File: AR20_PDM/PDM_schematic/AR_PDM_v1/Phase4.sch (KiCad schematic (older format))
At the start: 22 parts, among them Q1 BTS50025-1TAD, U1 INA233

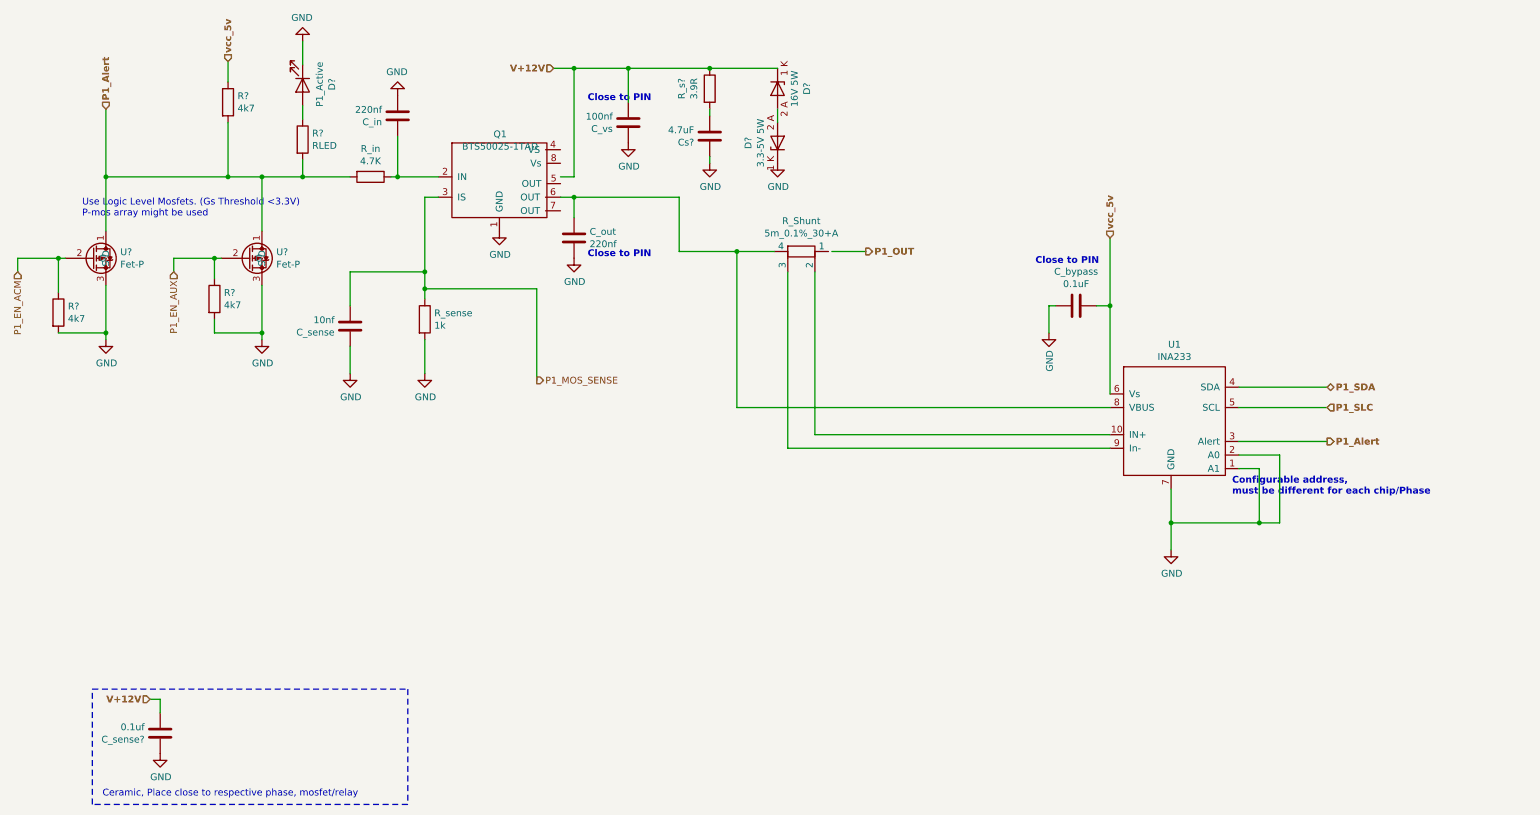
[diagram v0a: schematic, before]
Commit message: Major Schematics changes-work in progress
- Added rest of the phases
- Corrected pin names, and began to connect everything
- Began mapping the connectors, Pin-out not yet verified for all connectors
- Began mapping of user interface (Led indicators)
- INA233 now senses OUT voltage on mosfets instead of main 12Volt
- Added extra decoupling capacitors
Known things to fix:
- AUX inputs activation method, and a disconnect switch on phase 1-7 (mosfets)
- Rest of the user interface
- Find correct plugs for the system
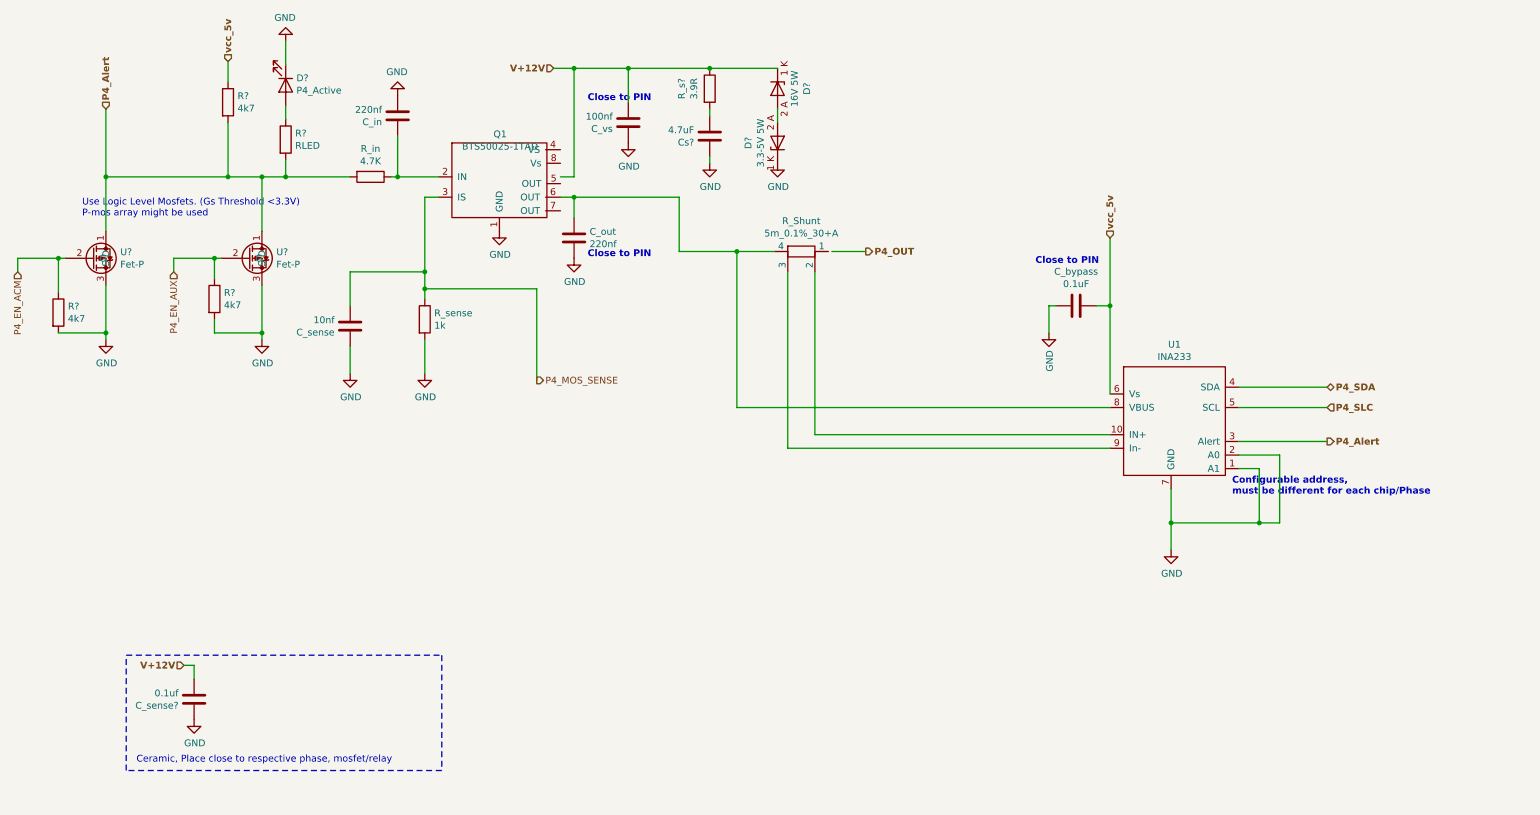
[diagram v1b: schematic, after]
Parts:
- removed C_sense?: 0.1uf, symbol AR20_PDM_v1-rescue:C-Device
- removed D?: P1_Active, symbol Device:LED
- removed R?: RLED, symbol AR20_PDM_v1-rescue:R-Device
- added C_sense?: 0.1uf, symbol AR20_PDM_v1-rescue:C-Device
- added D?: P4_Active, symbol Device:LED
- added R?: RLED, symbol AR20_PDM_v1-rescue:R-Device
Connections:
- net GND: now also C_sense?.1, D?.1 (K)
- net V+12V: now also C_sense?.2
- net P1_Alert renamed P4_Alert
- net P4_Alert: now also R?.2
- net P1_EN_ACM renamed P4_EN_ACM
- net P1_EN_AUX renamed P4_EN_AUX
- net P1_MOS_SENSE renamed P4_MOS_SENSE
- net P1_SDA renamed P4_SDA
- net P1_SLC renamed P4_SLC
- new net: D?.2 (A), R?.1

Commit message: Added LEDs and switches.
- Added all status leds
- Added all switches
- ! Connections are work in progress, not everything is correct
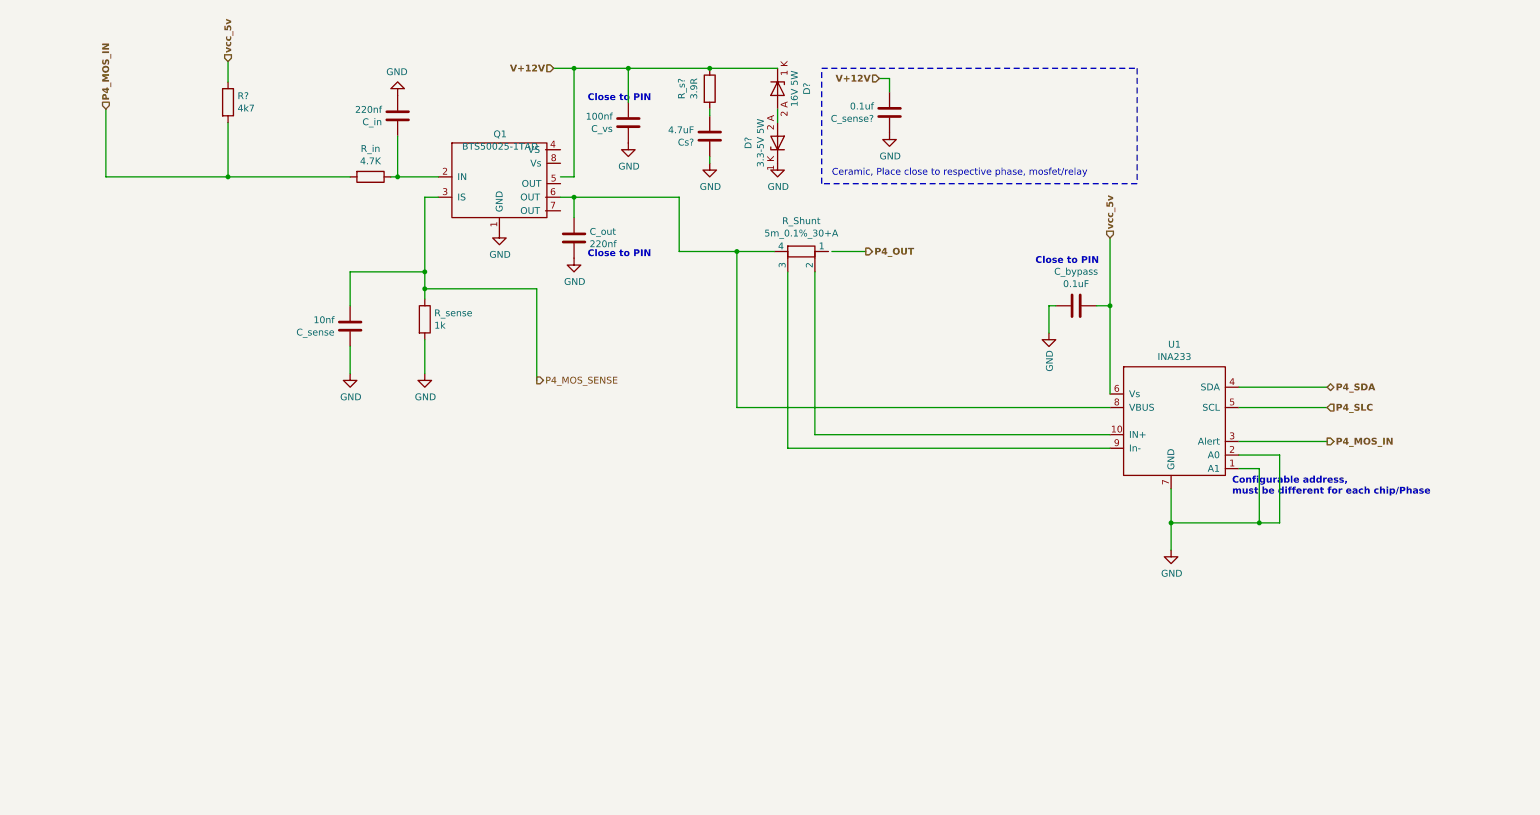
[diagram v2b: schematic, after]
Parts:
- removed D?: P4_Active, symbol Device:LED
- removed R? (x2): 4k7, symbol AR20_PDM_v1-rescue:R-Device
- removed R?: RLED, symbol AR20_PDM_v1-rescue:R-Device
- removed U? (x2): Fet-P, symbol AR20_PDM_v1-rescue:GenericFet-P
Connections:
- net labels added: P4_MOS_IN
- net labels removed: P4_Alert, P4_EN_ACM, P4_EN_AUX
- wire segments 81 -> 59
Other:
- note removed: "Use Logic Level Mosfets. (Gs Threshold <3.3V)\nP-mos array might be used"
- moved on the sheet: C_sense?

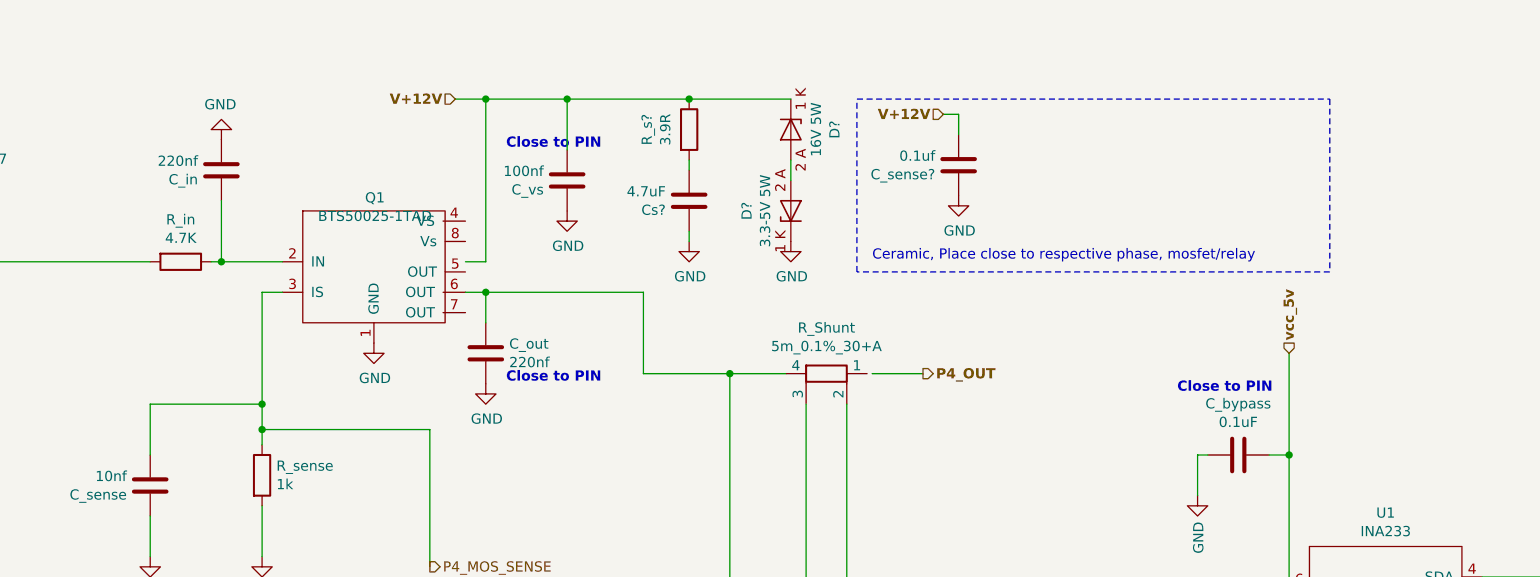
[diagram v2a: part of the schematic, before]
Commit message: Fixed wrong value components and ports, wiring, see discription
- Fixed supply cappacitor value 220 nf to 100nf
- Fixed IN cappacitor value 220 nf to 150 nf
- Fixed out cappacitor value, 220nf to 10 nf
- Made a mux for mosfet sense
- Found a I/O port expander
- Added some and removed some leds
- Fixed all labels, and wired everything up, besides the connectors
- Still missing connector and acm connector pinout.
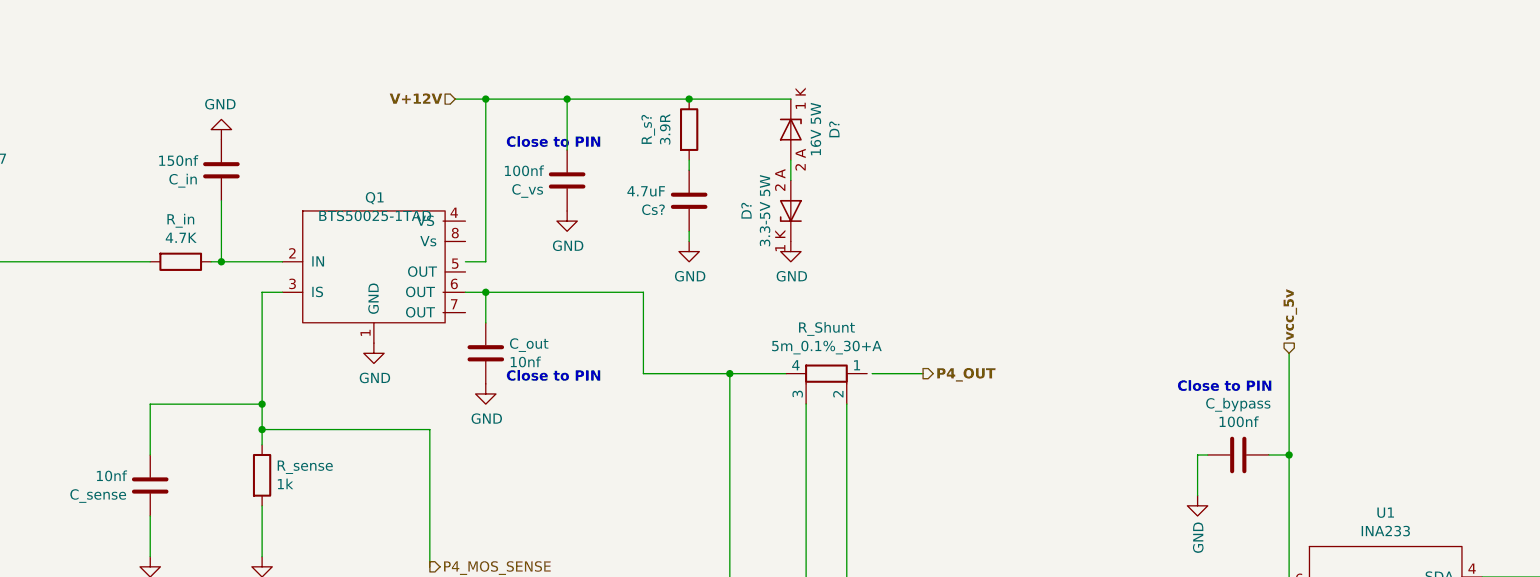
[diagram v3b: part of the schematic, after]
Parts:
- removed C_sense?: 0.1uf, symbol AR20_PDM_v1-rescue:C-Device
- C_bypass: value 0.1uF -> 100nf
- C_in: value 220nf -> 150nf
- C_out: value 220nf -> 10nf
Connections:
- wire segments 59 -> 57
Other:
- note removed: "Ceramic, Place close to respective phase, mosfet/relay"
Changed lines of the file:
@@
 $Descr A4 11693 8268
 encoding utf-8
-Sheet 9 11
+Sheet 9 13
 Title ""
 Date ""
@@
 AR Path="/5E10174B/5DAAC1D1" Ref="C_out?"  Part="1"
 F 0 "C_out?" H 4915 2896 50  0000 L CNN
-F 1 "220nf" H 4915 2805 50  0000 L CNN
+F 1 "10nf" H 4915 2805 50  0000 L CNN
 F 2 "" H 4838 2700 50  0001 C CNN
 F 3 "~" H 4800 2850 50  0001 C CNN
@@
 AR Path="/5E10174B/5DAAC1D7" Ref="C_in?"  Part="1"
 F 0 "C_in?" H 3615 1996 50  0000 L CNN
-F 1 "220nf" H 3615 1905 50  0000 L CNN
+F 1 "150nf" H 3615 1905 50  0000 L CNN
 F 2 "" H 3538 1800 50  0001 C CNN
 F 3 "~" H 3500 1950 50  0001 C CNN
@@
 	1    3700 3850
 	1    0    0    -1
-$EndComp
-$Comp
-L AR20_PDM_v1-rescue:C-Device C_bypass
-U 1 1 5DAAC201
-P 8500 3350
-AR Path="/5DA89415/5DAAC201" Ref="C_bypass"  Part="1"
-AR Path="/5DEB10A1/5DAAC201" Ref="C_bypass?"  Part="1"
-AR Path="/5DEB20EA/5DAAC201" Ref="C_bypass?"  Part="1"
-AR Path="/5E0E4725/5DAAC201" Ref="C_bypass?"  Part="1"
-AR Path="/5E0E4A93/5DAAC201" Ref="C_bypass?"  Part="1"
-AR Path="/5E0E4EB5/5DAAC201" Ref="C_bypass?"  Part="1"
-AR Path="/5E0E5304/5DAAC201" Ref="C_bypass?"  Part="1"
-AR Path="/5E0E594B/5DAAC201" Ref="C_bypass?"  Part="1"
-AR Path="/5E0E607C/5DAAC201" Ref="C_bypass?"  Part="1"
-AR Path="/5E0FB5C8/5DAAC201" Ref="C_bypass?"  Part="1"
-AR Path="/5E0FBBBD/5DAAC201" Ref="C_bypass?"  Part="1"
-AR Path="/5E0FC3A2/5DAAC201" Ref="C_bypass?"  Part="1"
-AR Path="/5E0FCFDC/5DAAC201" Ref="C_bypass?"  Part="1"
-AR Path="/5E0FDCCC/5DAAC201" Ref="C_bypass?"  Part="1"
-AR Path="/5E10174B/5DAAC201" Ref="C_bypass?"  Part="1"
-F 0 "C_bypass?" V 8248 3350 50  0000 C CNN
-F 1 "0.1uF" V 8339 3350 50  0000 C CNN
-F 2 "" H 8538 3200 50  0001 C CNN
-F 3 "~" H 8500 3350 50  0001 C CNN
-	1    8500 3350
-	0    1    1    0
 $EndComp
 Wire Wire Line
@@
 Text HLabel 4650 1600 0    50   Input ~ 10
 V+12V
-$Comp
-L AR20_PDM_v1-rescue:C-Device C_sense?
-U 1 1 5E1AB1BE
-P 7125 1925
-AR Path="/5DA89415/5E1AB1BE" Ref="C_sense?"  Part="1"
-AR Path="/5DEB10A1/5E1AB1BE" Ref="C_sense?"  Part="1"
-AR Path="/5DEB20EA/5E1AB1BE" Ref="C_sense?"  Part="1"
-AR Path="/5E0E4725/5E1AB1BE" Ref="C_sense?"  Part="1"
-AR Path="/5E0E4A93/5E1AB1BE" Ref="C_sense?"  Part="1"
-AR Path="/5E0E4EB5/5E1AB1BE" Ref="C_sense?"  Part="1"
-AR Path="/5E0E5304/5E1AB1BE" Ref="C_sense?"  Part="1"
-AR Path="/5E0E594B/5E1AB1BE" Ref="C_sense?"  Part="1"
-AR Path="/5E0E607C/5E1AB1BE" Ref="C_sense?"  Part="1"
-AR Path="/5E0FB5C8/5E1AB1BE" Ref="C_sense?"  Part="1"
-AR Path="/5E0FBBBD/5E1AB1BE" Ref="C_sense?"  Part="1"
-AR Path="/5E0FC3A2/5E1AB1BE" Ref="C_sense?"  Part="1"
-AR Path="/5E0FCFDC/5E1AB1BE" Ref="C_sense?"  Part="1"
-AR Path="/5E0FDCCC/5E1AB1BE" Ref="C_sense?"  Part="1"
-AR Path="/5E10174B/5E1AB1BE" Ref="C_sense?"  Part="1"
-F 0 "C_sense?" H 7240 1971 50  0000 L CNN
-F 1 "0.1uf" H 7240 1880 50  0000 L CNN
-F 2 "" H 7163 1775 50  0001 C CNN
-F 3 "~" H 7125 1925 50  0001 C CNN
-	1    7125 1925
-	-1   0    0    1
-$EndComp
-$Comp
-L AR20_PDM_v1-rescue:GND-power #PWR?
-U 1 1 5E1AB1C4
-P 7125 2075
-AR Path="/5DA89415/5E1AB1C4" Ref="#PWR?"  Part="1"
-AR Path="/5DEB10A1/5E1AB1C4" Ref="#PWR?"  Part="1"
-AR Path="/5DEB20EA/5E1AB1C4" Ref="#PWR?"  Part="1"
-AR Path="/5E0E4725/5E1AB1C4" Ref="#PWR?"  Part="1"
-AR Path="/5E0E4A93/5E1AB1C4" Ref="#PWR?"  Part="1"
-AR Path="/5E0E4EB5/5E1AB1C4" Ref="#PWR?"  Part="1"
-AR Path="/5E0E5304/5E1AB1C4" Ref="#PWR?"  Part="1"
-AR Path="/5E0E594B/5E1AB1C4" Ref="#PWR?"  Part="1"
-AR Path="/5E0E607C/5E1AB1C4" Ref="#PWR?"  Part="1"
-AR Path="/5E0FB5C8/5E1AB1C4" Ref="#PWR?"  Part="1"
-AR Path="/5E0FBBBD/5E1AB1C4" Ref="#PWR?"  Part="1"
-AR Path="/5E0FC3A2/5E1AB1C4" Ref="#PWR?"  Part="1"
-AR Path="/5E0FCFDC/5E1AB1C4" Ref="#PWR?"  Part="1"
-AR Path="/5E0FDCCC/5E1AB1C4" Ref="#PWR?"  Part="1"
-AR Path="/5E10174B/5E1AB1C4" Ref="#PWR?"  Part="1"
-F 0 "#PWR?" H 7125 1825 50  0001 C CNN
-F 1 "GND" H 7130 1902 50  0000 C CNN
-F 2 "" H 7125 2075 50  0001 C CNN
-F 3 "" H 7125 2075 50  0001 C CNN
-	1    7125 2075
-	1    0    0    -1
-$EndComp
-Wire Wire Line
-	7125 1775 7125 1675
-Wire Wire Line
-	7125 1675 7050 1675
-Text Notes 6700 2400 0    50   ~ 0
-Ceramic, Place close to respective phase, mosfet/relay
-Text HLabel 7050 1675 0    50   Input ~ 10
-V+12V
-Wire Notes Line
-	6625 1600 8950 1600
-Wire Notes Line
-	8950 1600 8950 2450
-Wire Notes Line
-	8950 2450 6625 2450
-Wire Notes Line
-	6625 2450 6625 1600
 Wire Wire Line
 	2250 2400 3150 2400
+$Comp
+L AR20_PDM_v1-rescue:C-Device C_bypass
+U 1 1 5DAAC201
+P 8500 3350
+AR Path="/5DA89415/5DAAC201" Ref="C_bypass"  Part="1"
+AR Path="/5DEB10A1/5DAAC201" Ref="C_bypass?"  Part="1"
+AR Path="/5DEB20EA/5DAAC201" Ref="C_bypass?"  Part="1"
+AR Path="/5E0E4725/5DAAC201" Ref="C_bypass?"  Part="1"
+AR Path="/5E0E4A93/5DAAC201" Ref="C_bypass?"  Part="1"
+AR Path="/5E0E4EB5/5DAAC201" Ref="C_bypass?"  Part="1"
+AR Path="/5E0E5304/5DAAC201" Ref="C_bypass?"  Part="1"
+AR Path="/5E0E594B/5DAAC201" Ref="C_bypass?"  Part="1"
+AR Path="/5E0E607C/5DAAC201" Ref="C_bypass?"  Part="1"
+AR Path="/5E0FB5C8/5DAAC201" Ref="C_bypass?"  Part="1"
+AR Path="/5E0FBBBD/5DAAC201" Ref="C_bypass?"  Part="1"
+AR Path="/5E0FC3A2/5DAAC201" Ref="C_bypass?"  Part="1"
+AR Path="/5E0FCFDC/5DAAC201" Ref="C_bypass?"  Part="1"
+AR Path="/5E0FDCCC/5DAAC201" Ref="C_bypass?"  Part="1"
+AR Path="/5E10174B/5DAAC201" Ref="C_bypass?"  Part="1"
+F 0 "C_bypass?" V 8248 3350 50  0000 C CNN
+F 1 "100nf" V 8339 3350 50  0000 C CNN
+F 2 "" H 8538 3200 50  0001 C CNN
+F 3 "~" H 8500 3350 50  0001 C CNN
+	1    8500 3350
+	0    1    1    0
+$EndComp
 $EndSCHEMATC
